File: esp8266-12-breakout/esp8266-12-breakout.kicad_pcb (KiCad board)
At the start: 2 copper layers, 12 parts, among them P1 ftdi, P2 CONN_01X14, P3 power, SW1 SW_PUSH, U1 AP1117D33, U2 esp8266-12

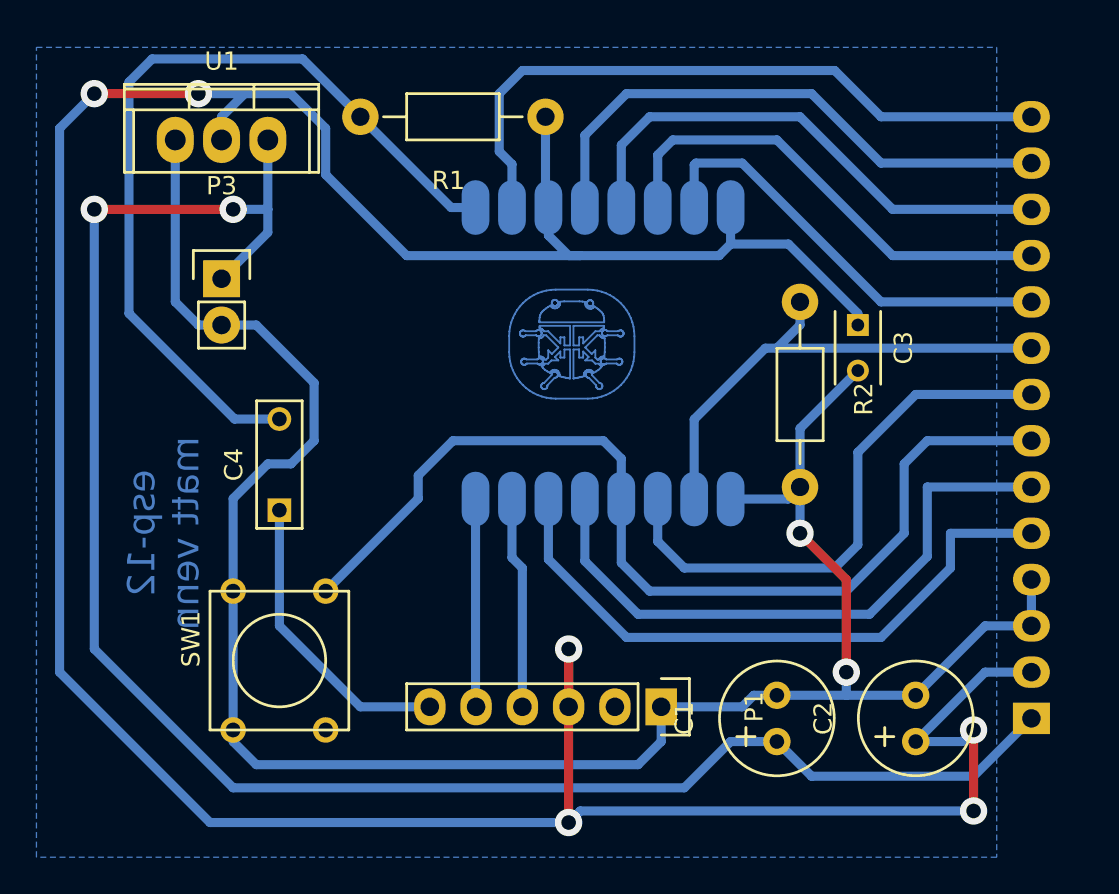
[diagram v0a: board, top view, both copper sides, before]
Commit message: better pin ordering
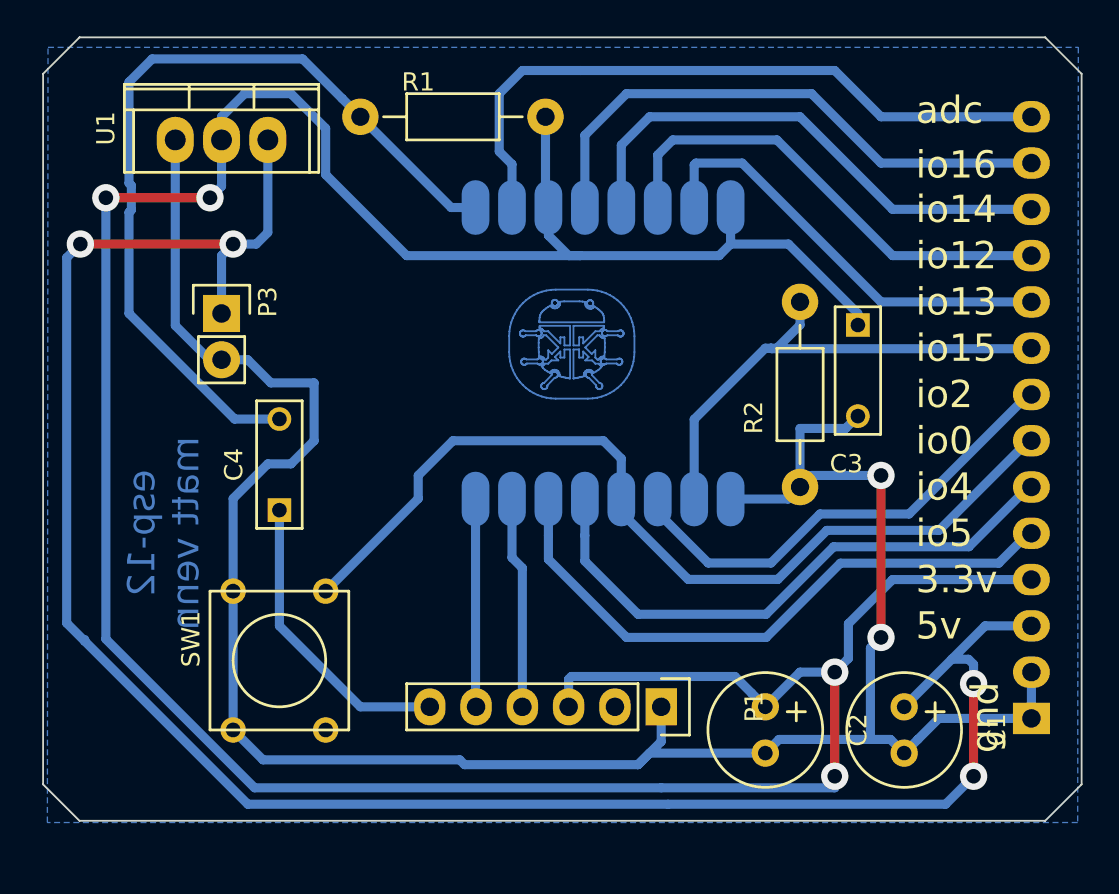
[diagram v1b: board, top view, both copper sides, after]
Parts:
- C3: footprint Capacitors_ThroughHole:C_Rect_L4_W2.5_P2.5 -> Capacitors_ThroughHole:C_Rect_L7_W2.5_P5
- P2: footprint Pin_Headers:Pin_Header_Angled_1x14 -> Pin_Headers:Pin_Header_Straight_1x14
- moved C2 8.47 mm to (93.3, 137.2), turned to 270 degrees
- moved C1 7.24 mm to (101.0, 137.2), turned to 270 degrees
- moved P3 1.90 mm to (63.5, 115.6)
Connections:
- P2 pad 1: +5V -> GND
- P2 pad 2: +3V3 -> GND
- P2 pad 3: GND -> +5V
- P2 pad 4: GND -> +3V3
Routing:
- net +5V: track 100.1 -> 111.7 mm, vias 2 -> 4
- net +3V3: track 178.3 -> 169.9 mm, vias 6 -> 4
- net GND: track 116.0 -> 123.5 mm
- net /gpio0: track 55.3 -> 50.9 mm
- net /gpio2: track 30.4 -> 26.2 mm
- net /gpio4: track 34.2 -> 32.0 mm
- net /gpio5: track 35.1 -> 34.0 mm
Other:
- board outline added: 57 x 43 mm
- net class etch: clearance 0.3 -> 0.4
- board text added: "3.3v"
- board text added: "5v"
- board text added: "adc"
- board text added: "gnd"
- board text added: "io0"
- board text added: "io12"
- board text added: "io13"
- board text added: "io14"
- board text added: "io15"
- board text added: "io16"
- board text added: "io2"
- board text added: "io4"
- board text added: "io5"
